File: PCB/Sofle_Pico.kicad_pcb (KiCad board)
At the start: 2 copper layers, 164.6 x 116.3 mm, 85 parts, among them J2 MJ-4PP-9, Q1 Si2301CDS, SW1 SW_PUSH, SW10 SW_PUSH, SW11 SW_PUSH, SW12 SW_PUSH, SW13 SW_PUSH, SW14 SW_PUSH, SW15 SW_PUSH, SW16 SW_PUSH, SW17 SW_PUSH, SW18 SW_PUSH, SW19 SW_PUSH, SW2 SW_PUSH, SW20 SW_PUSH, SW21 SW_PUSH, SW22 SW_PUSH, SW23 SW_PUSH, SW24 SW_PUSH, SW25 SW_PUSH, SW26 SW_PUSH, SW27 SW_PUSH, SW28 SW_PUSH, SW29 SW_PUSH, SW3 SW_PUSH, SW30 SW_PUSH, SW31 SW_PUSH, SW32 SW_PUSH, SW33 SW_PUSH, SW34 SW_PUSH, SW35 SW_PUSH, SW36 SW_PUSH, SW4 SW_PUSH, SW5 SW_PUSH, SW6 SW_PUSH, SW7 SW_PUSH, SW8 SW_PUSH, SW9 SW_PUSH, U2 Pico

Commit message: second board is not smart
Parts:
- removed C1: 1uF, Capacitor_SMD:C_0805_2012Metric_Pad1.18x1.45mm_HandSolder
- removed C2, C3, C4: 0.1uF, Capacitor_SMD:C_0805_2012Metric_Pad1.18x1.45mm_HandSolder
- removed D32, D33, D34, D35, D36, D37: D, Sofle_Pico:D_SOD-123_DO-35_Hybrid_DoubleSided_V2
- removed G***: LOGO, Sofle_Pico:RH_Print_Logo
- removed G***: LOGO, Sofle_Pico:LH_Print
- removed JP2: SolderJumper_2_Open, Sofle_Pico:Level Shifter Bypass Jumper
- removed Q1: Si2301CDS, Sofle_Pico:SOT-23_DS
- removed R3, R4: 2.2k, Sofle_Pico:Res_1206_SMD_6.3mm_TH_Hybrid
- removed SW31, SW32, SW33, SW34, SW35, SW36: SW_PUSH, Sofle_Pico:Cherry_MX_DS_Hotswap_v3.5.4
- added D38: D, Sofle_Pico:D_SOD-123_DO-35_Hybrid_DoubleSided_V2, F.Cu at (234.0, 83.6)
- added D39: D, Sofle_Pico:D_SOD-123_DO-35_Hybrid_DoubleSided_V2, F.Cu at (233.6, 99.6)
- added D40: D, Sofle_Pico:D_SOD-123_DO-35_Hybrid_DoubleSided_V2, F.Cu at (235.0, 115.5)
- added D41: D, Sofle_Pico:D_SOD-123_DO-35_Hybrid_DoubleSided_V2, F.Cu at (234.6, 139.0)
- added J1: Conn_02x08_Top_Bottom, Connector_PinHeader_1.27mm:PinHeader_2x08_P1.27mm_Horizontal, B.Cu at (90.1, 88.2)
- added J3: Conn_01x06, Connector_PinHeader_1.27mm:PinHeader_1x06_P1.27mm_Horizontal, B.Cu at (100.7, 133.5)
- added SW37: SW_PUSH, Sofle_Pico:Cherry_MX_DS_Hotswap_v3.5.4, B.Cu at (234.8, 52.4)
- added SW38: SW_PUSH, Sofle_Pico:Cherry_MX_DS_Hotswap_v3.5.4, B.Cu at (234.8, 71.5)
- added SW39: SW_PUSH, Sofle_Pico:Cherry_MX_DS_Hotswap_v3.5.4, B.Cu at (234.8, 90.5)
- added SW40: SW_PUSH, Sofle_Pico:Cherry_MX_DS_Hotswap_v3.5.4, B.Cu at (234.8, 109.5)
- added SW41: SW_PUSH, Sofle_Pico:Cherry_MX_DS_Hotswap_v3.5.4, B.Cu at (234.8, 128.6)
- D31: value MBR120VLSF -> D; footprint Sofle_Pico:D_SOD-123_DO-41_7.62mm_Hybrid_DoubleSided -> Sofle_Pico:D_SOD-123_DO-35_Hybrid_DoubleSided_V2
- J2: value MJ-4PP-9 -> Conn_02x08_Top_Bottom; footprint Sofle_Pico:MJ-4PP-9 -> Connector_PinHeader_1.27mm:PinHeader_2x08_P1.27mm_Horizontal
- U2: footprint Sofle_Pico:RPi_Pico_SMD_TH_DS -> Module:RaspberryPi_Pico_SMD_HandSolder; moved to B.Cu
- moved D31 152.2 mm to (234.1, 63.0), turned to 0 degrees
- moved J2 13.5 mm to (94.1, 95.8), turned to 180 degrees
- moved D30 5.97 mm to (215.6, 138.5)
- moved SW30 5.69 mm to (215.8, 128.6)
- moved SW29 5.69 mm to (196.8, 128.6)
- moved D29 4.97 mm to (196.6, 137.5)
- moved D28 4.12 mm to (177.1, 133.5)
- moved SW28 3.79 mm to (177.7, 123.7)
- moved SW25 3.23 mm to (120.5, 126.2)
- moved D26 3.16 mm to (139.9, 134.0)
- moved D25 3.00 mm to (120.9, 135.0)
- moved SW26 1.75 mm to (139.6, 123.7)
- moved D27 1.58 mm to (158.6, 131.5)
- moved SW27 1.52 mm to (158.7, 121.2)
- moved U2 0.26 mm to (96.3, 60.4), turned to 180 degrees
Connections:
- D31 pad 1: VSYS -> row0
- D31 pad 2: VBUS -> Net-(D31-A)
- J2 pad 1: GND -> lcol0
- J2 pad 2: Net-(JP2-A) -> lcol1
- J2 pad 3: TX -> lcol2
- J2 pad 4: RX -> lcol3
- SW1 pad 1: col5 -> lcol0
- SW10 pad 1: col2 -> lcol3
- SW11 pad 1: col1 -> lcol4
- SW12 pad 1: col0 -> lcol5
- SW13 pad 1: col5 -> lcol0
- SW14 pad 1: col4 -> lcol1
- SW15 pad 1: col3 -> lcol2
- SW16 pad 1: col2 -> lcol3
- SW17 pad 1: col1 -> lcol4
- SW18 pad 1: col0 -> lcol5
- SW19 pad 1: col5 -> lcol0
- SW2 pad 1: col4 -> lcol1
- SW20 pad 1: col4 -> lcol1
- SW21 pad 1: col3 -> lcol2
- SW22 pad 1: col2 -> lcol3
- SW23 pad 1: col1 -> lcol4
- SW24 pad 1: col0 -> lcol5
- SW25 pad 2: col5 -> lcol0
- SW26 pad 2: col4 -> lcol1
- SW27 pad 1: col3 -> lcol2
- SW28 pad 1: col2 -> lcol3
- SW29 pad 1: col1 -> lcol4
- SW3 pad 1: col3 -> lcol2
- SW30 pad 1: col0 -> lcol5
- SW4 pad 1: col2 -> lcol3
- SW5 pad 1: col1 -> lcol4
- SW6 pad 1: col0 -> lcol5
- SW7 pad 1: col5 -> lcol0
- SW8 pad 1: col4 -> lcol1
- SW9 pad 1: col3 -> lcol2
- U2 pad 1: unconnected-(U2-GPIO0-Pad1) -> lcol0
- U2 pad 11: col5 -> unconnected-(U2-GPIO8-Pad11)
- U2 pad 12: row0 -> unconnected-(U2-GPIO9-Pad12)
- U2 pad 14: row1 -> row0
- U2 pad 15: row2 -> row1
- U2 pad 16: row3 -> row2
- U2 pad 17: row4 -> row3
- U2 pad 19: unconnected-(U2-GPIO14-Pad19) -> row4
- U2 pad 2: col0 -> lcol1
- U2 pad 20: unconnected-(U2-GPIO15-Pad20) -> row5
- U2 pad 21: TX -> unconnected-(U2-GPIO16-Pad21)
- U2 pad 22: RX -> unconnected-(U2-GPIO17-Pad22)
- U2 pad 24: GP18 -> unconnected-(U2-GPIO18-Pad24)
- U2 pad 25: GP19 -> rcol6
- U2 pad 26: GP20 -> rcol5
- U2 pad 27: GP21 -> rcol4
- U2 pad 29: GP22 -> rcol3
- U2 pad 31: GP26 -> rcol2
- U2 pad 32: GP27 -> rcol1
- U2 pad 34: GP28 -> rcol0
- U2 pad 4: col1 -> lcol2
- U2 pad 5: col2 -> lcol3
- U2 pad 6: col3 -> lcol4
- U2 pad 7: col4 -> lcol5
- U2 pad 9: unconnected-(U2-GPIO6-Pad9)_1 -> lcol6
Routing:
- net col0: track 244.8 -> 0.00 mm
- net col1: track 225.9 -> 0.00 mm
- net col2: track 207.6 -> 0.00 mm
- net col3: track 203.1 -> 0.00 mm, vias 2 -> 0
- net col4: track 198.0 -> 0.00 mm
- net row3: track 165.5 -> 0.00 mm
- net row2: track 148.0 -> 0.00 mm, vias 3 -> 0
- net row4: track 132.4 -> 0.00 mm
- net row1: track 130.9 -> 0.00 mm, vias 3 -> 0
- net row0: track 129.0 -> 0.00 mm, vias 2 -> 0
- net 3V3: track 102.0 -> 0.00 mm, vias 1 -> 0
- net col5: track 93.7 -> 0.00 mm
- net VBUS: track 81.7 -> 0.00 mm, vias 1 -> 0
- net GP18: track 67.9 -> 0.00 mm
- net Net-(D26-A): track 30.1 -> 0.00 mm
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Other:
- outline, holes or cut-outs redrawn
- board text removed: "LH"
- board text removed: "RH"

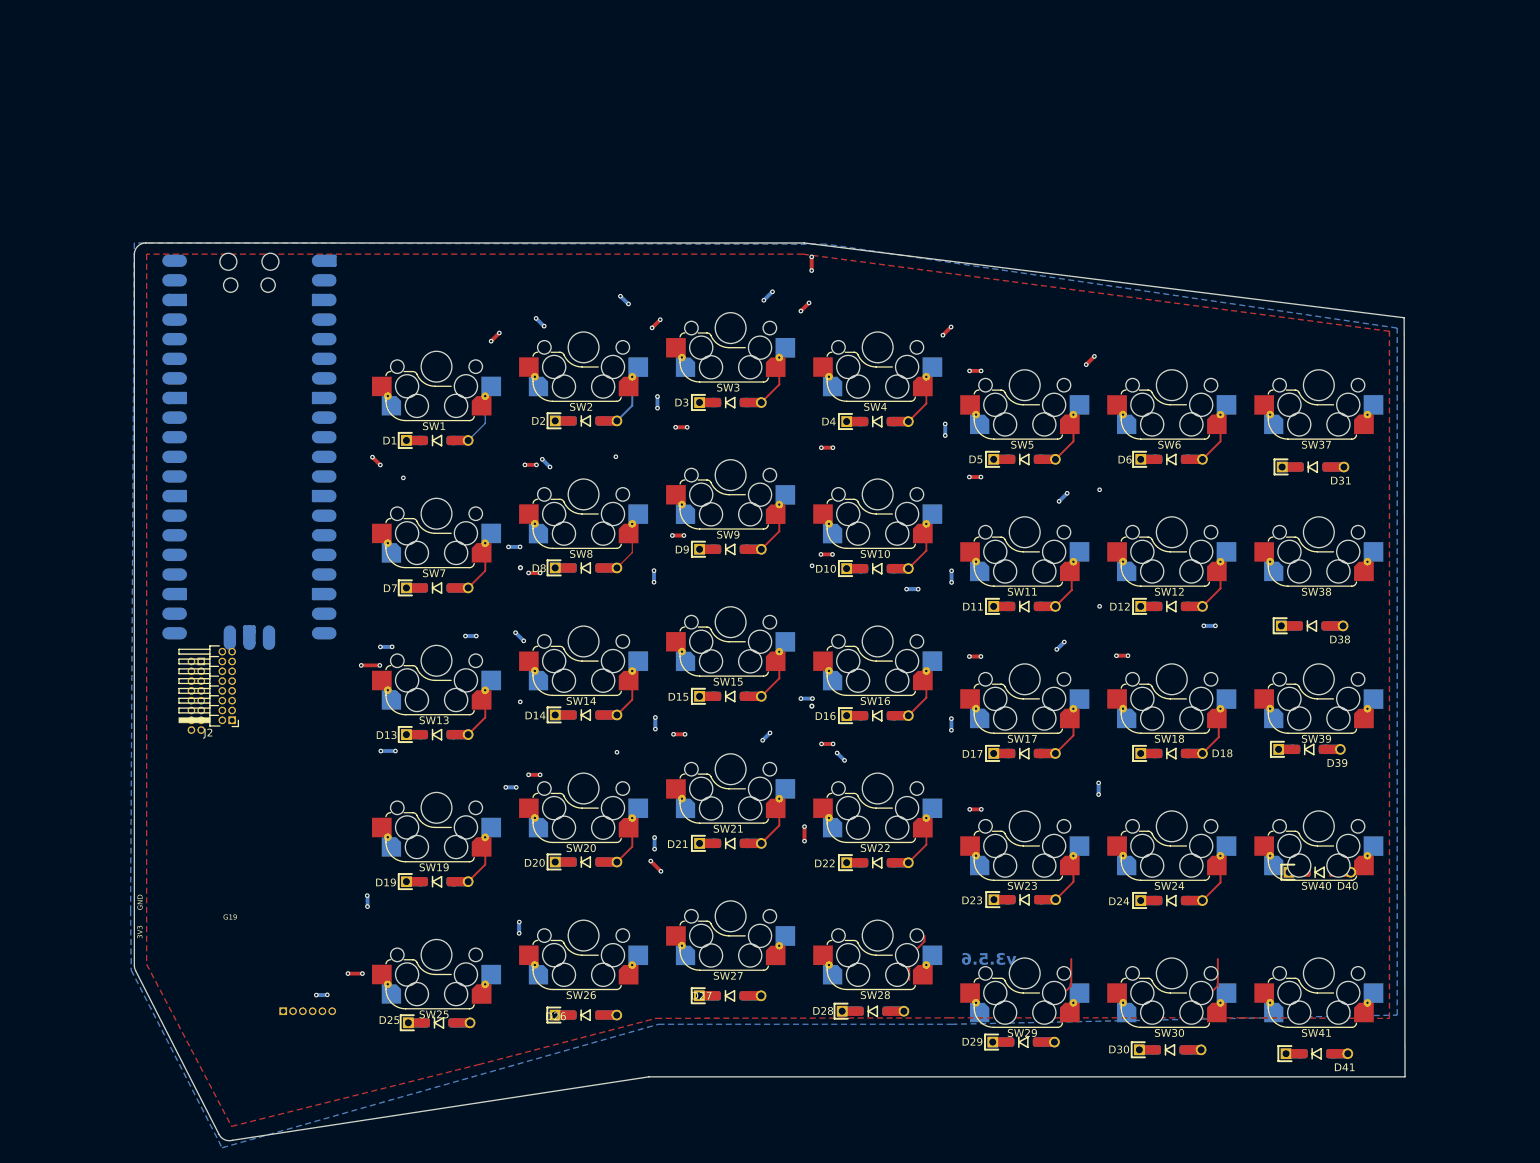
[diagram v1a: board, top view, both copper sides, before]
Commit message: chop off unneeded keys
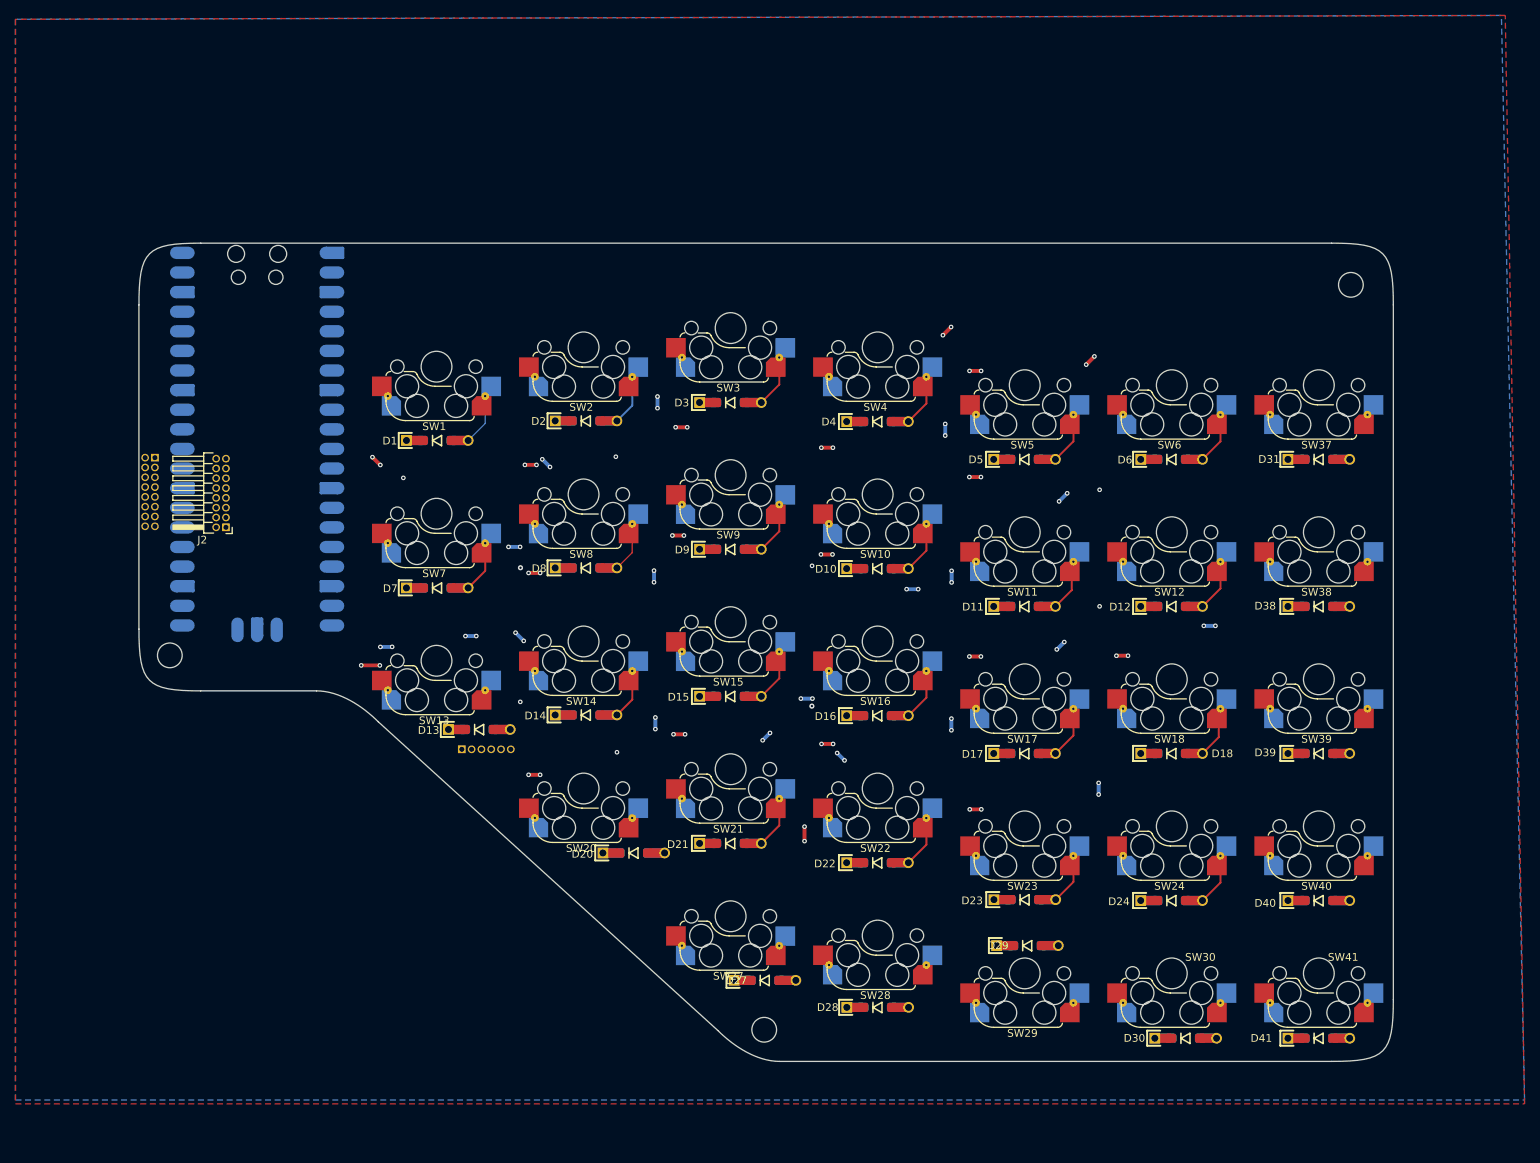
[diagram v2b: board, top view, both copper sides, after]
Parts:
- removed D19, D25, D26: D, Sofle_Pico:D_SOD-123_DO-35_Hybrid_DoubleSided_V2
- removed SW19, SW25, SW26: SW_PUSH, Sofle_Pico:Cherry_MX_DS_Hotswap_v3.5.4
- D31, D38, D39, D40, D41: moved to B.Cu
- moved J3 41.1 mm to (123.8, 99.6)
- moved J1 27.1 mm to (84.1, 61.8)
- moved J2 25.0 mm to (93.3, 70.8)
- moved D29 12.5 mm to (197.1, 125.0)
- moved D20 6.29 mm to (146.1, 113.0)
- moved D13 5.49 mm to (126.1, 97.0)
- moved D27 4.92 mm to (163.1, 129.5)
- moved D40 3.66 mm to (234.8, 119.2)
- moved D38 2.66 mm to (234.8, 81.1)
- moved D30 2.50 mm to (217.6, 137.0)
- moved D41 2.02 mm to (234.8, 137.0)
- moved U2 1.43 mm to (97.3, 59.4)
- moved D39 1.32 mm to (234.8, 100.1)
- moved D31 1.24 mm to (234.8, 62.0)
- moved D28 0.78 mm to (177.7, 133.0)
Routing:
- net VSYS: track 41.5 -> 27.9 mm, vias 56 -> 38
- net GND: track 39.7 -> 29.7 mm, vias 50 -> 38
- net Net-(D30-A): track 6.77 -> 0.00 mm
- net Net-(D29-A): track 6.77 -> 0.00 mm
- net Net-(D19-A): track 6.67 -> 0.00 mm
- net Net-(D13-A): track 6.67 -> 0.00 mm
- net Net-(D20-A): track 6.53 -> 0.00 mm
- net Net-(D28-A): track 6.52 -> 0.00 mm
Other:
- board size 164.6 x 116.3 mm -> 162.5 x 106 mm
- board text removed: "${REVISION}"
- board text removed: "3V3"
- board text removed: "G19"
- board text removed: "GND"
